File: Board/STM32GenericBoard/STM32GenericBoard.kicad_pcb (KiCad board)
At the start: 6 copper layers, 50.8 x 50.8 mm, 62 parts, among them J1 USB_B_Micro, J2 Conn_01x08_Pin, U1 STM32H743VGTx, U2 AMS1117-3.3, U3 ICM-45686, Y1 Crystal_GND24

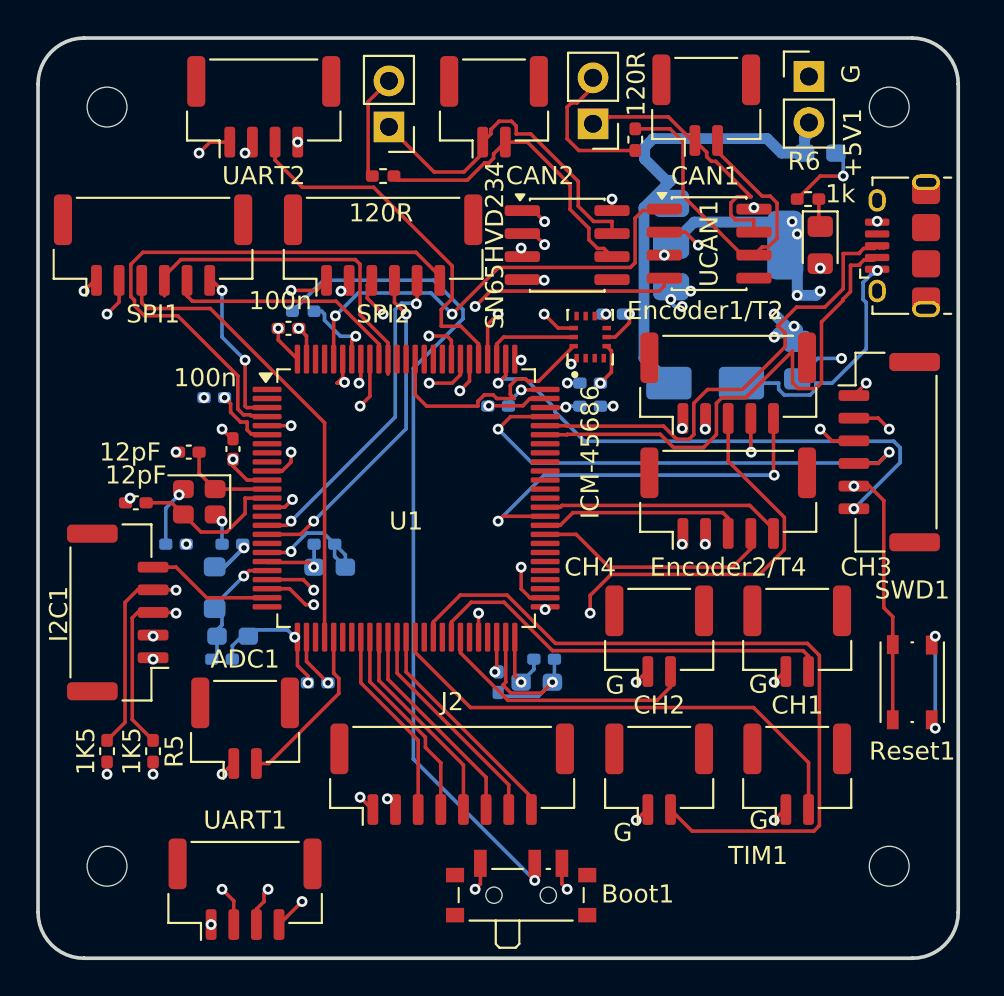
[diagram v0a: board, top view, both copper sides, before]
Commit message: feat(telemetry): add WiFi UDP bridge and UART4 DMA streaming
Add ESP32 bridge, TelemetryServer, and STM32 BalanceFrame at 200 Hz/921600.

Fix UART4 TC IRQ for HAL DMA TX completion, RPC gain tuning, and NVIC setup.

Co-authored-by: Cursor <cursoragent@cursor.com>
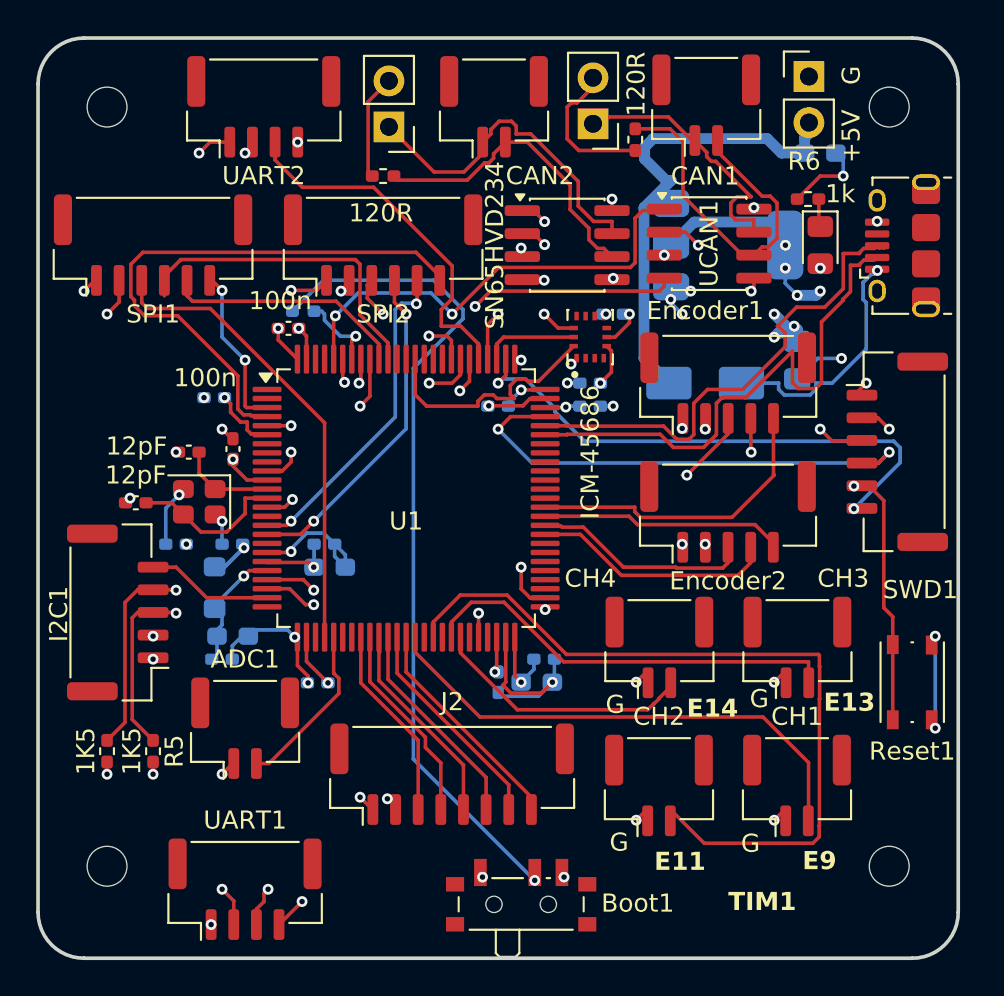
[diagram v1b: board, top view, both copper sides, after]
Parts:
- moved Encoder2 0.76 mm to (128.3, 51.6)
- moved CH1 0.62 mm to (132.1, 66.7)
- moved CH2 0.62 mm to (124.4, 66.7)
- moved CH4 0.62 mm to (124.5, 59.0)
- moved CH3 0.62 mm to (132.1, 59.0)
- moved Boot1 0.51 mm to (116.8, 72.9)
- moved SWD1 0.45 mm to (137.6, 48.2)
- renumbered +5V1 to +5V, Encoder1/T2 to Encoder1, Encoder2/T4 to Encoder2
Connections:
- Encoder1 pad 5: TIM4_Z -> TIM2_Z
- Encoder2 pad 5: TIM2_Z -> TIM4_Z
- UCAN1 pad 5: unconnected-(UCAN1-Vref-Pad5) -> +3V3
- UCAN1 pad 8: +3V3 -> GND
- UCAN2 pad 5: unconnected-(UCAN2-Vref-Pad5) -> +3V3
- UCAN2 pad 8: +3V3 -> GND
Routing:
- net TIM4_Z: track 22.1 -> 13.4 mm, vias 2 -> 0
- net TIM2_CH2: track 40.4 -> 32.8 mm
- net TIM2_Z: track 13.4 -> 17.1 mm
- net +3V3: track 56.1 -> 53.2 mm
- net TIM1_CH2: track 42.4 -> 43.3 mm
- net SPI1_MISO: track 19.1 -> 18.3 mm
- net UART4_RX: track 37.5 -> 36.8 mm
- net TIM4_CH2: track 11.4 -> 12.0 mm
- net GND: track 79.1 -> 78.7 mm, vias 41 -> 43
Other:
- board text added: "A2"
- board text added: "A2 CL DA + G"
- board text added: "E11"
- board text added: "E13"
- board text added: "E14"
- board text added: "E9"
